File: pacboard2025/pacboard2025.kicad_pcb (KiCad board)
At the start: 4 copper layers, 80 x 85 mm, 30 parts, among them J1 XT30 Male Connector, U2 D24V50F5, U3 ProS3

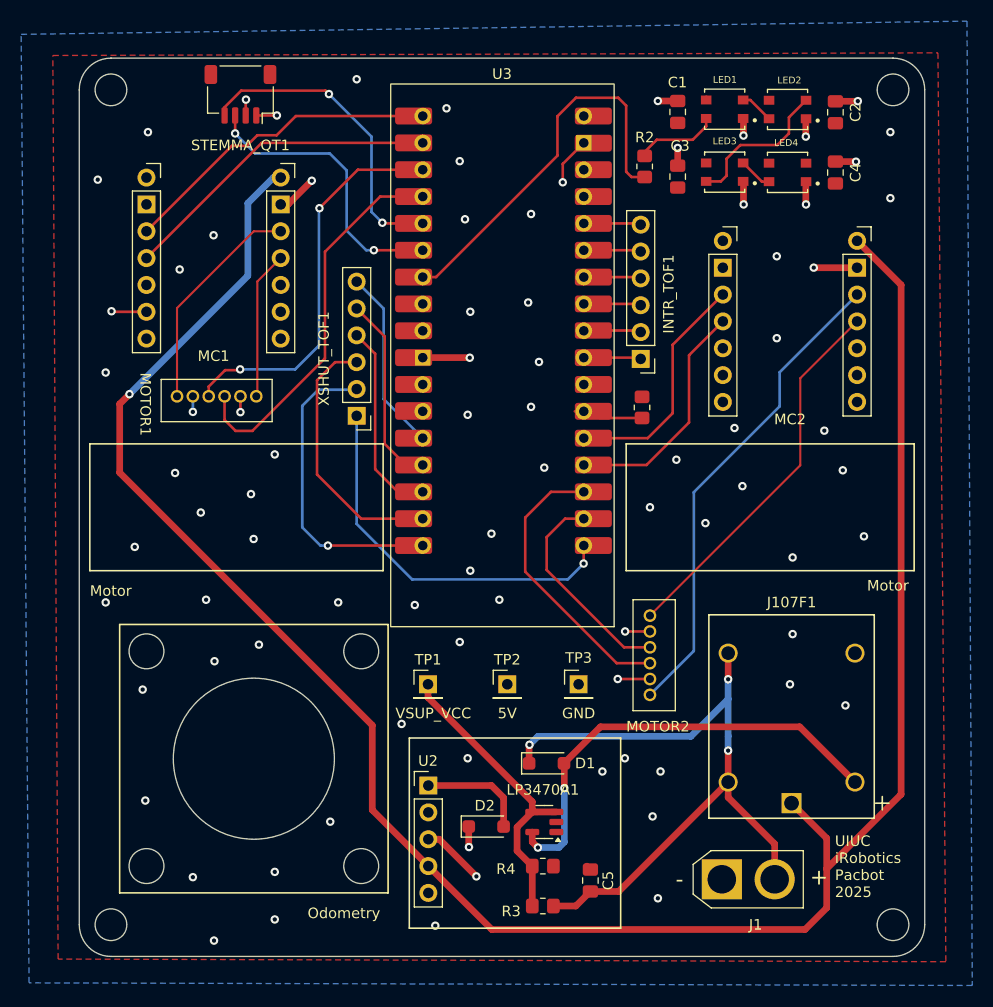
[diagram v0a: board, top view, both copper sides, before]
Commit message: some minor changes to traces
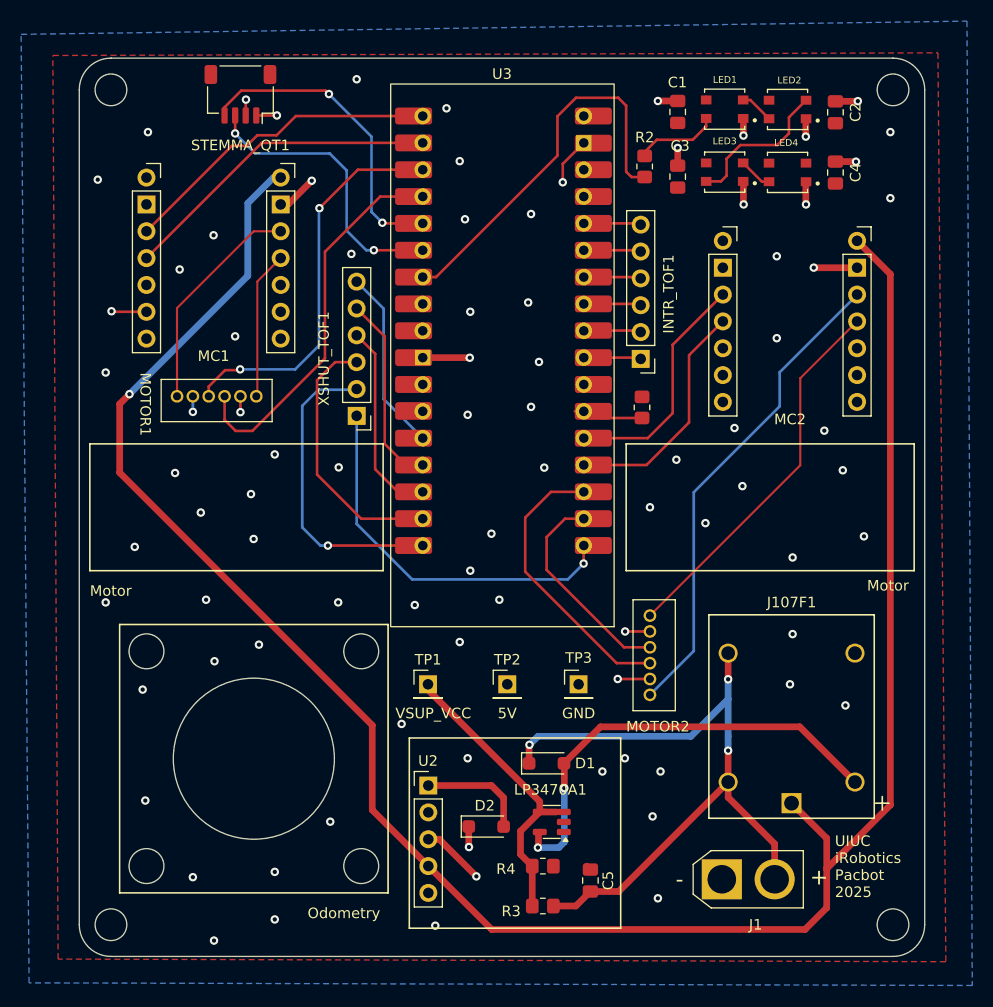
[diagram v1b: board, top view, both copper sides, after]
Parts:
- moved LP3470A1 0.71 mm to (156.3, 133.6)
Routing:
- net /12V: track 200.3 -> 199.5 mm
- net /GND: vias 71 -> 74
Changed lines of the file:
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@@
 	(footprint "Package_TO_SOT_SMD:SOT-23-5"
 		(layer "F.Cu")
-		(at 155.5525 133.555 180)
+		(at 156.2625 133.55 180)
 		(descr "SOT, 5 Pin (https://www.jedec.org/sites/default/files/docs/Mo-178c.PDF variant AA), generated with kicad-footprint-generator ipc_gullwing_generator.py")
 		(tags "SOT TO_SOT_SMD")
@@
 	)
 	(via
+		(at 126.3 87.6)
+		(size 0.8)
+		(drill 0.4)
+		(layers "F.Cu" "B.Cu")
+		(net 4)
+	)
+	(via
 		(at 123.55 112.525)
 		(size 0.8)
@@
 	)
 	(via
+		(at 137.3 79.8)
+		(size 0.8)
+		(drill 0.4)
+		(layers "F.Cu" "B.Cu")
+		(net 4)
+	)
+	(via
 		(at 155.05 90.025)
 		(size 0.8)
@@
 	)
 	(via
+		(at 136.1 100)
+		(size 0.8)
+		(drill 0.4)
+		(layers "F.Cu" "B.Cu")
+		(net 4)
+	)
+	(via
 		(at 148.55 109.775)
 		(size 0.8)
@@
 	)
 	(segment
-		(start 154.415 134.505)
-		(end 154.415 135.44)
+		(start 157.45 130.35)
+		(end 157.45 128.04)
 		(width 0.635)
 		(layer "F.Cu")
@@
 	)
 	(segment
-		(start 154.415 135.44)
-		(end 154.95 135.975)
+		(start 160.87 124.55)
+		(end 179.724998 124.55)
 		(width 0.635)
 		(layer "F.Cu")
@@
 	)
 	(segment
-		(start 157.45 130.35)
-		(end 157.45 128.04)
+		(start 154.95 135.975)
+		(end 155 135.925)
 		(width 0.635)
 		(layer "F.Cu")
@@
 	)
 	(segment
-		(start 160.87 124.55)
-		(end 179.724998 124.55)
+		(start 155 135.925)
+		(end 155 134.625)
 		(width 0.635)
 		(layer "F.Cu")
@@
 	)
 	(segment
+		(start 155 134.625)
+		(end 155.125 134.5)
+		(width 0.635)
+		(layer "F.Cu")
+		(net 12)
+	)
+	(segment
 		(start 157.45 128.04)
 		(end 157.415 128.005)
@@
 	)
 	(segment
-		(start 156.925 135.975)
-		(end 157.45 135.45)
+		(start 157.45 135.45)
+		(end 157.45 130.35)
 		(width 0.635)
 		(layer "B.Cu")
@@
 	)
 	(segment
-		(start 157.45 135.45)
-		(end 157.45 130.35)
+		(start 156.925 135.975)
+		(end 157.45 135.45)
 		(width 0.635)
 		(layer "B.Cu")
@@
 	)
 	(segment
-		(start 150.58 143.725)
-		(end 180.225 143.725)
+		(start 185.15 78.5675)
+		(end 188.3 81.7175)
 		(width 0.635)
 		(layer "F.Cu")
@@
 	)
 	(segment
-		(start 185.15 78.5675)
-		(end 189.3175 82.735)
+		(start 150.58 143.725)
+		(end 180.225 143.725)
 		(width 0.635)
 		(layer "F.Cu")
@@
 	)
 	(segment
-		(start 189.3175 82.735)
-		(end 189.3175 130.9325)
-		(width 0.635)
-		(layer "F.Cu")
-		(net 14)
-	)
-	(segment
 		(start 115.375 100.5)
 		(end 139.275 124.4)
@@
 	)
 	(segment
-		(start 189.3175 130.9325)
+		(start 188.3 131.95)
 		(end 182.275 137.975)
 		(width 0.635)
@@
 		(net 14)
 	)
+	(segment
+		(start 188.3 81.7175)
+		(end 188.3 131.95)
+		(width 0.635)
+		(layer "F.Cu")
+		(net 14)
+	)
 	(via
 		(at 116.3 93.075)
@@
 	)
 	(segment
-		(start 152.975 134.045)
-		(end 152.975 136.29)
+		(start 144.55 121.05)
+		(end 155.125 131.625)
 		(width 0.635)
 		(layer "F.Cu")
@@
 	)
 	(segment
-		(start 154.415 141.505)
+		(start 155.125 132.6)
+		(end 155.13 132.605)
+		(width 0.635)
+		(layer "F.Cu")
+		(net 42)
+	)
+	(segment
+		(start 153.3 136.615)
 		(end 154.415 137.73)
 		(width 0.635)
@@
 	)
 	(segment
-		(start 154.415 131.64)
-		(end 154.415 132.605)
+		(start 154.415 141.505)
+		(end 154.415 137.73)
 		(width 0.635)
 		(layer "F.Cu")
@@
 	)
 	(segment
-		(start 154.415 132.605)
+		(start 155.13 132.605)
 		(end 156.69 132.605)
 		(width 0.635)
@@
 	)
 	(segment
-		(start 152.975 136.29)
-		(end 154.415 137.73)
+		(start 155.125 132.6)
+		(end 153.3 134.425)
 		(width 0.635)
 		(layer "F.Cu")
@@
 	(segment
 		(start 144.55 120.525)
-		(end 144.55 121.775)
+		(end 144.55 121.05)
 		(width 0.635)
 		(layer "F.Cu")
@@
 	)
 	(segment
-		(start 144.55 121.775)
-		(end 154.415 131.64)
+		(start 155.125 131.625)
+		(end 155.125 132.6)
 		(width 0.635)
 		(layer "F.Cu")
@@
 	)
 	(segment
-		(start 154.415 132.605)
-		(end 152.975 134.045)
+		(start 153.3 134.425)
+		(end 153.3 136.615)
 		(width 0.635)
 		(layer "F.Cu")

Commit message: some more minor adjustments
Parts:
- moved INTR_TOF1 1.23 mm to (165.9, 89.6)
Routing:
- net /INTR_TOF1: track 4.53 -> 5.87 mm
- net /INTR_TOF3: track 4.53 -> 5.71 mm
- net /INTR_TOF6: track 4.53 -> 5.71 mm
- net /INTR_TOF2: track 4.53 -> 5.71 mm
- net /INTR_TOF5: track 4.54 -> 5.72 mm
- net /INTR_TOF4: track 4.53 -> 5.71 mm
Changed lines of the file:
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@@
 	(footprint "Connector_PinHeader_2.54mm:PinHeader_1x06_P2.54mm_Vertical"
 		(layer "F.Cu")
-		(at 164.675 89.735 180)
+		(at 165.9 89.61 180)
 		(descr "Through hole straight pin header, 1x06, 2.54mm pitch, single row")
 		(tags "Through hole pin header THT 1x06 2.54mm single row")
@@
 	)
 	(segment
-		(start 164.555 81.995)
-		(end 164.675 82.115)
+		(start 165.895 81.995)
+		(end 165.9 81.99)
 		(width 0.254)
 		(layer "F.Cu")
@@
 	(segment
 		(start 160.1925 81.995)
-		(end 164.555 81.995)
+		(end 165.895 81.995)
 		(width 0.254)
 		(layer "F.Cu")
@@
 	(segment
 		(start 160.1925 84.53)
-		(end 164.55 84.53)
+		(end 165.9 84.53)
 		(width 0.254)
 		(layer "F.Cu")
@@
 	)
 	(segment
-		(start 164.55 84.53)
-		(end 164.675 84.655)
-		(width 0.254)
-		(layer "F.Cu")
-		(net 6)
-	)
-	(segment
-		(start 164.53 87.05)
-		(end 164.675 87.195)
+		(start 165.88 87.05)
+		(end 165.9 87.07)
 		(width 0.254)
 		(layer "F.Cu")
@@
 	(segment
 		(start 160.1925 87.05)
-		(end 164.53 87.05)
+		(end 165.88 87.05)
 		(width 0.254)
 		(layer "F.Cu")
@@
 	)
 	(segment
-		(start 160.1925 79.455)
-		(end 164.555 79.455)
+		(start 165.895 79.455)
+		(end 165.9 79.45)
 		(width 0.254)
 		(layer "F.Cu")
@@
 	)
 	(segment
-		(start 164.555 79.455)
-		(end 164.675 79.575)
+		(start 160.1925 79.455)
+		(end 165.895 79.455)
 		(width 0.254)
 		(layer "F.Cu")
@@
 	(segment
 		(start 160.1925 89.615)
-		(end 164.555 89.615)
+		(end 165.895 89.615)
 		(width 0.25)
 		(layer "F.Cu")
@@
 	)
 	(segment
-		(start 164.555 89.615)
-		(end 164.675 89.735)
+		(start 165.895 89.615)
+		(end 165.9 89.61)
 		(width 0.25)
 		(layer "F.Cu")
@@
 	)
 	(segment
-		(start 164.555 76.915)
-		(end 164.675 77.035)
+		(start 165.685 77.035)
+		(end 165.8 76.92)
 		(width 0.254)
 		(layer "F.Cu")
@@
 	)
 	(segment
+		(start 165.9 76.91)
+		(end 164.56 76.91)
+		(width 0.25)
+		(layer "F.Cu")
+		(net 10)
+	)
+	(segment
+		(start 164.56 76.91)
+		(end 164.555 76.915)
+		(width 0.25)
+		(layer "F.Cu")
+		(net 10)
+	)
+	(segment
 		(start 160.1925 76.915)
 		(end 164.555 76.915)
@@
 	)
 	(segment
-		(start 167.7 88.3975)
-		(end 167.7 94.875)
+		(start 172.45 83.6475)
+		(end 168.3 87.7975)
 		(width 0.25)
 		(layer "F.Cu")
@@
 	)
 	(segment
-		(start 172.45 83.6475)
-		(end 167.7 88.3975)
+		(start 168.3 87.7975)
+		(end 168.3 94.275)
 		(width 0.25)
 		(layer "F.Cu")
@@
 	)
 	(segment
-		(start 167.7 94.875)
+		(start 168.3 94.275)
 		(end 165.34 97.235)
 		(width 0.25)

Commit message: some more misc changes
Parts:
- LED1, LED2, LED3, LED4: footprint board1_footprints:Neopixel -> board1_footprints:Neopixels 5050
- moved C2 3.45 mm to (186.1, 68.1)
- moved C4 3.07 mm to (186.0, 73.1)
- moved LED4 2.22 mm to (180.6, 73.0), turned to 0 degrees
- moved LED2 2.17 mm to (180.7, 66.1), turned to 0 degrees
- moved C1 0.89 mm to (167.3, 66.2)
- moved LED3 0.76 mm to (172.8, 72.8), turned to 0 degrees
- moved C3 0.63 mm to (167.6, 72.8)
- turned LED1 to 0 degrees
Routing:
- net Net-(LED2-DOUT): track 14.5 -> 18.7 mm
- net /SERIAL_DATA_LINE: track 27.4 -> 31.0 mm, vias 2 -> 1
- net /+3.3V: track 14.4 -> 11.7 mm, vias 4 -> 3
- net /GND: track 31.1 -> 33.4 mm
- net Net-(D1-A): track 42.9 -> 44.9 mm
- net Net-(LED1-DOUT): track 3.21 -> 4.87 mm
- net /5V: track 17.1 -> 18.7 mm
- net Net-(LED3-DOUT): track 3.19 -> 4.70 mm
- net Net-(LED1-DIN): track 7.94 -> 6.52 mm
- net /SERIAL_CLOCK_LINE: track 28.7 -> 29.2 mm, vias 2 -> 1

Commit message: some more tiny changes
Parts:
- moved LED3 0.20 mm to (172.8, 73.0)
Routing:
- net /12V: track 199.5 -> 198.7 mm
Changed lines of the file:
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@@
 	(footprint "board1_footprints:Neopixels 5050"
 		(layer "F.Cu")
-		(at 172.8 72.8)
+		(at 172.8 73)
 		(tags "1655 ")
 		(property "Reference" "LED3"
@@
 		)
 		(property "Footprint" "board1_footprints:Neopixels 5050"
-			(at 0 0 360)
+			(at 0 0 0)
 			(layer "F.Fab")
 			(hide yes)
@@
 		)
 		(property "Datasheet" ""
-			(at 0 0 360)
+			(at 0 0 0)
 			(layer "F.Fab")
 			(hide yes)
@@
 		)
 		(property "Description" ""
-			(at 0 0 360)
+			(at 0 0 0)
 			(layer "F.Fab")
 			(hide yes)
@@
 		)
 		(property "Footprint" "board1_footprints:Neopixels 5050"
-			(at 0 0 360)
+			(at 0 0 0)
 			(layer "F.Fab")
 			(hide yes)
@@
 		)
 		(property "Datasheet" ""
-			(at 0 0 360)
+			(at 0 0 0)
 			(layer "F.Fab")
 			(hide yes)
@@
 		)
 		(property "Description" ""
-			(at 0 0 360)
+			(at 0 0 0)
 			(layer "F.Fab")
 			(hide yes)
@@
 		)
 		(property "Footprint" "board1_footprints:Neopixels 5050"
-			(at 0 0 360)
+			(at 0 0 0)
 			(layer "F.Fab")
 			(hide yes)
@@
 		)
 		(property "Datasheet" ""
-			(at 0 0 360)
+			(at 0 0 0)
 			(layer "F.Fab")
 			(hide yes)
@@
 		)
 		(property "Description" ""
-			(at 0 0 360)
+			(at 0 0 0)
 			(layer "F.Fab")
 			(hide yes)
@@
 		)
 		(property "Footprint" "board1_footprints:Neopixels 5050"
-			(at 0 0 360)
+			(at 0 0 0)
 			(layer "F.Fab")
 			(hide yes)
@@
 		)
 		(property "Datasheet" ""
-			(at 0 0 360)
+			(at 0 0 0)
 			(layer "F.Fab")
 			(hide yes)
@@
 		)
 		(property "Description" ""
-			(at 0 0 360)
+			(at 0 0 0)
 			(layer "F.Fab")
 			(hide yes)
@@
 	)
 	(segment
-		(start 139.275 132.42)
-		(end 144.58 137.725)
+		(start 144.58 137.725)
+		(end 150.58 143.725)
 		(width 0.635)
 		(layer "F.Cu")
@@
 	)
 	(segment
-		(start 144.58 137.725)
-		(end 150.58 143.725)
+		(start 116.3 101.425)
+		(end 139.275 124.4)
 		(width 0.635)
 		(layer "F.Cu")
@@
 	)
 	(segment
-		(start 116.3 93.075)
-		(end 115.375 94)
-		(width 0.635)
-		(layer "F.Cu")
-		(net 14)
-	)
-	(segment
-		(start 115.375 94)
-		(end 115.375 100.5)
+		(start 139.275 124.4)
+		(end 139.275 132.42)
 		(width 0.635)
 		(layer "F.Cu")
@@
 	)
 	(segment
-		(start 115.375 100.5)
-		(end 139.275 124.4)
+		(start 116.3 93.075)
+		(end 116.3 101.425)
 		(width 0.635)
 		(layer "F.Cu")
@@
 	)
 	(segment
-		(start 139.275 124.4)
-		(end 139.275 132.42)
+		(start 182.275 137.975)
+		(end 182.275 135.099997)
 		(width 0.635)
 		(layer "F.Cu")
@@
 	)
 	(segment
-		(start 182.275 137.975)
-		(end 182.275 135.099997)
+		(start 188.3 81.7175)
+		(end 188.3 131.95)
 		(width 0.635)
 		(layer "F.Cu")
@@
 	)
 	(segment
-		(start 188.3 81.7175)
-		(end 188.3 131.95)
+		(start 139.275 132.42)
+		(end 144.58 137.725)
 		(width 0.635)
 		(layer "F.Cu")
@@
 	)
 	(segment
-		(start 181.1 65.9)
-		(end 182.55 64.45)
-		(width 0.25)
-		(layer "F.Cu")
-		(net 47)
-	)
-	(segment
 		(start 181.1 68.1)
 		(end 181.1 65.9)
@@
 	)
 	(segment
-		(start 170.375 74.425)
+		(start 170.375 74.625)
 		(end 170.375 73.525)
 		(width 0.25)
@@
 	)
 	(segment
-		(start 174.4 69.5)
-		(end 179.7 69.5)
+		(start 179.7 69.5)
+		(end 181.1 68.1)
 		(width 0.25)
 		(layer "F.Cu")
@@
 	)
 	(segment
-		(start 179.7 69.5)
-		(end 181.1 68.1)
+		(start 181.1 65.9)
+		(end 182.55 64.45)
+		(width 0.25)
+		(layer "F.Cu")
+		(net 47)
+	)
+	(segment
+		(start 174.4 69.5)
+		(end 179.7 69.5)
 		(width 0.25)
 		(layer "F.Cu")

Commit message: jonathan change bms
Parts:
- D2: footprint board1_footprints:SOD-123FL -> Diode_SMD:D_SMB
- moved D2 4.74 mm to (150.9, 133.6), turned to 90 degrees
- moved LP3470A1 2.05 mm to (158.3, 133.3)
- moved D1 1.99 mm to (157.9, 122.9)
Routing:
- net /GND: track 33.4 -> 27.6 mm, vias 74 -> 72
- net /+3.3V: track 11.7 -> 7.89 mm, vias 3 -> 1
- net Net-(D2-A): track 10.3 -> 7.46 mm
- net Net-(LP3470A1-VCC): track 28.1 -> 30.4 mm
- net /BAT_12V: track 67.0 -> 64.9 mm
- net Net-(D1-A): track 44.9 -> 42.9 mm

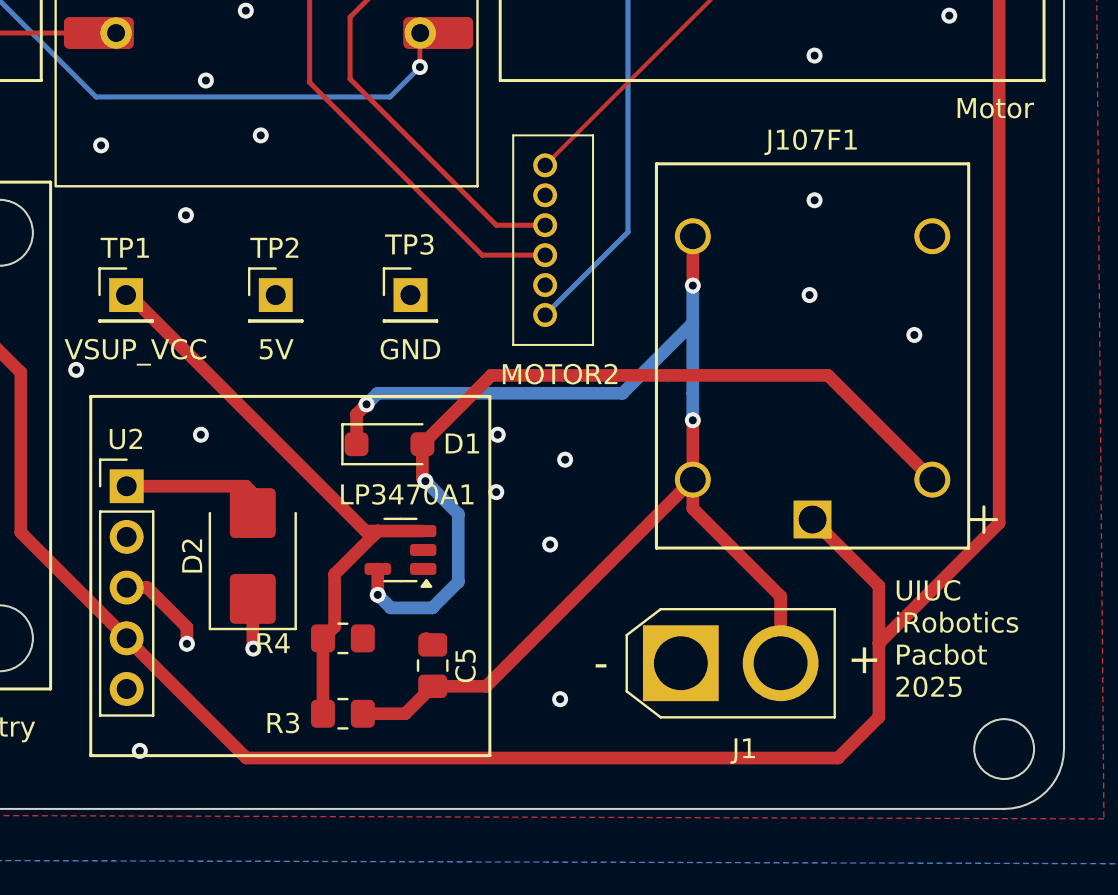
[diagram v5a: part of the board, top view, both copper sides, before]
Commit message: updated bms schematic and layout
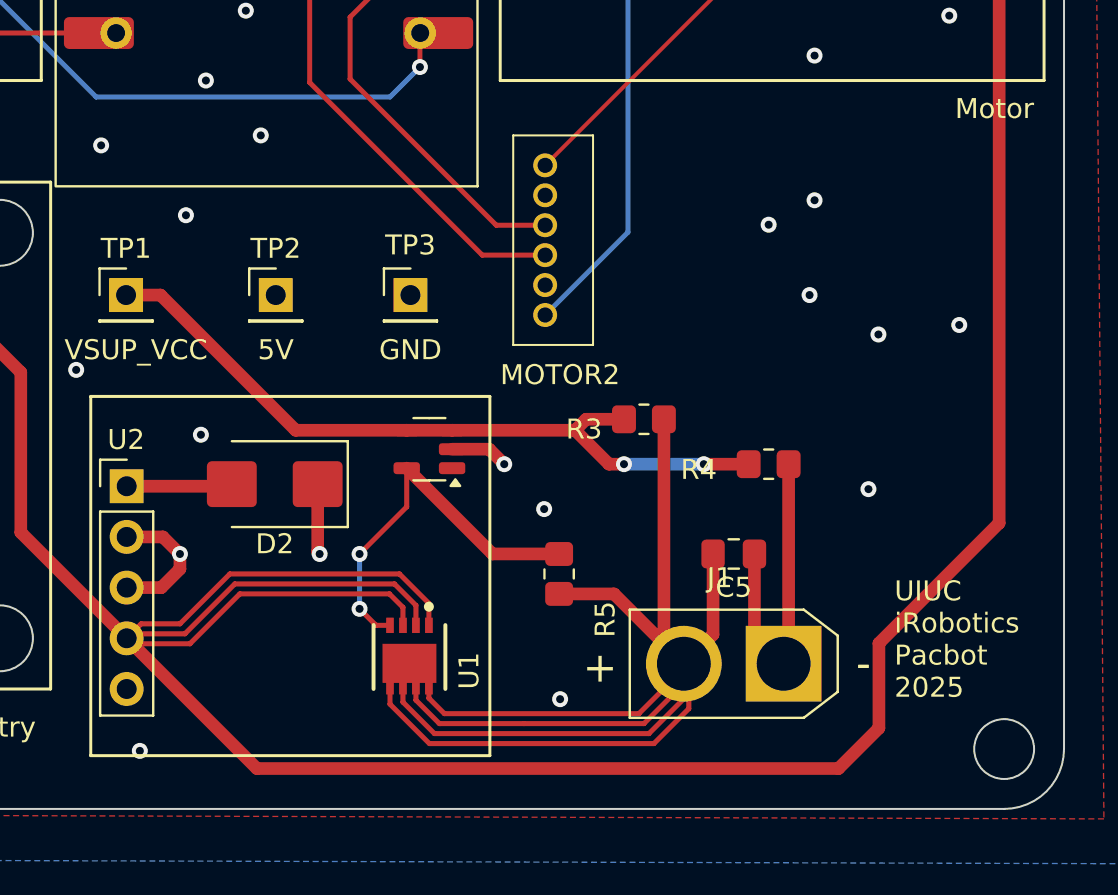
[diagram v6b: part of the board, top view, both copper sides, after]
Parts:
- removed D1: D, board1_footprints:SOD-123FL
- removed J107F1: ~, board1_footprints:J107
- added R5: 10K, Resistor_SMD:R_0805_2012Metric_Pad1.20x1.40mm_HandSolder, F.Cu at (166.2, 134.5)
- added U1: NMOS, board1_footprints:IFX-PG-TSDSON-8-901-G-V, F.Cu at (158.8, 138.7)
- R3: value 150k -> 15K
- R4: value 100k -> 10K
- moved R4 23.1 mm to (176.8, 129.0)
- moved R3 21.1 mm to (170.5, 126.8)
- moved C5 16.1 mm to (175.0, 133.5), turned to 180 degrees
- moved LP3470A1 5.25 mm to (159.8, 128.2)
- moved J1 5.15 mm to (177.5, 139.0), turned to 180 degrees
- moved D2 3.76 mm to (152.0, 130.0), turned to 180 degrees
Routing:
- net /12V: track 198.7 -> 243.3 mm
- net /BAT_12V: track 64.9 -> 95.1 mm, vias 3 -> 1
- net Net-(LP3470A1-RESET): track 42.9 -> 19.3 mm
- net /GND: track 27.6 -> 50.0 mm
- net Net-(LP3470A1-VCC): track 30.4 -> 37.4 mm, vias 0 -> 2
- net Net-(D2-A): track 7.46 -> 5.31 mm
- net /5V: track 18.7 -> 20.3 mm
